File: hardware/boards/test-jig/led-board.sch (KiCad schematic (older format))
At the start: 22 parts

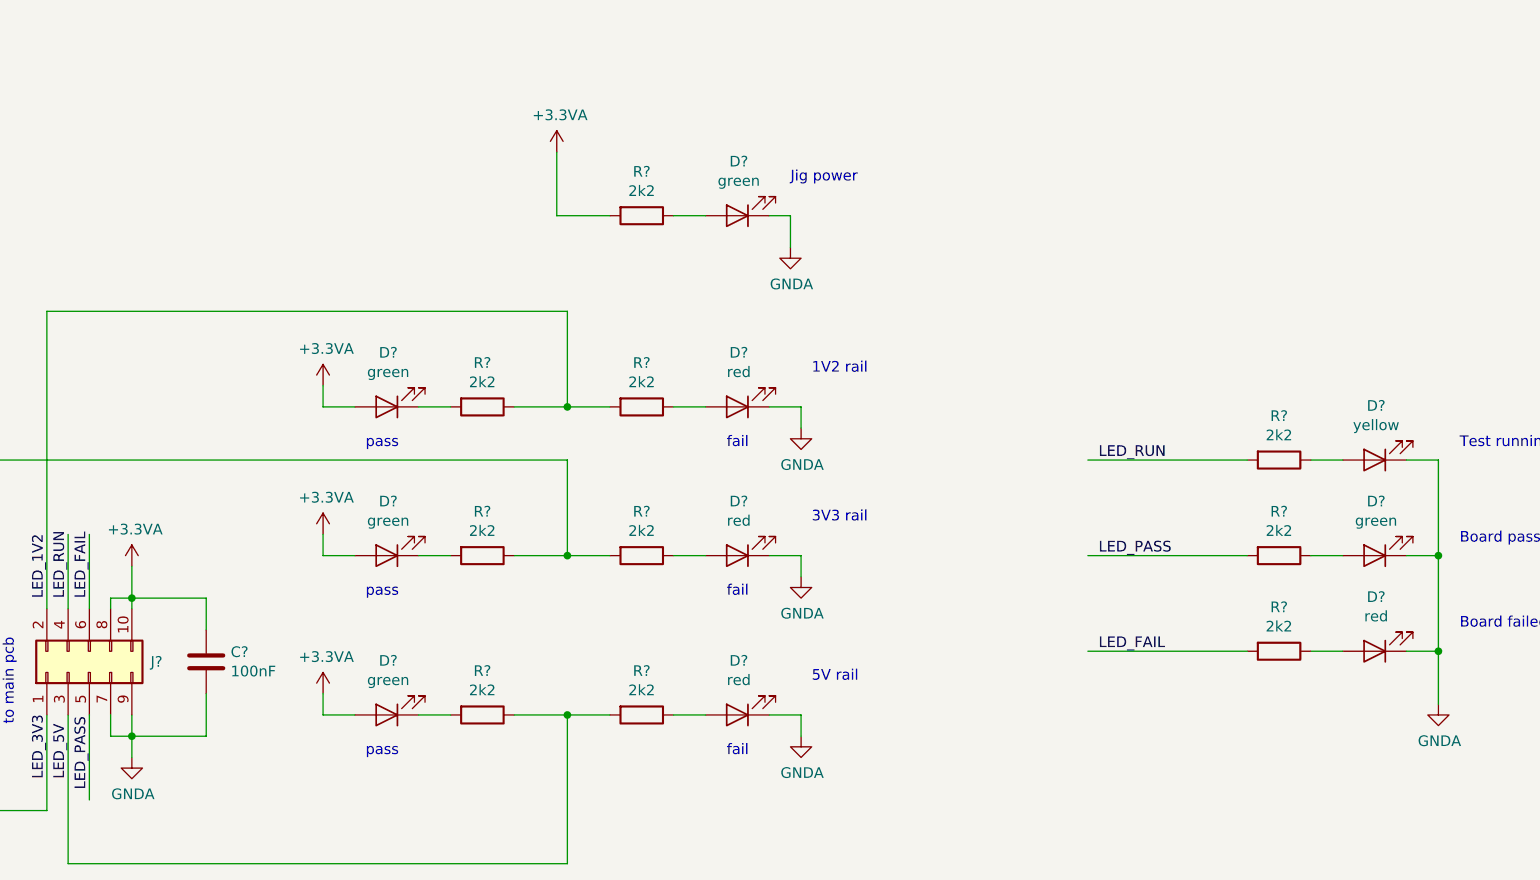
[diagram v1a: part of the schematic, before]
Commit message: test-jig schematics: annotate and ERC fixup
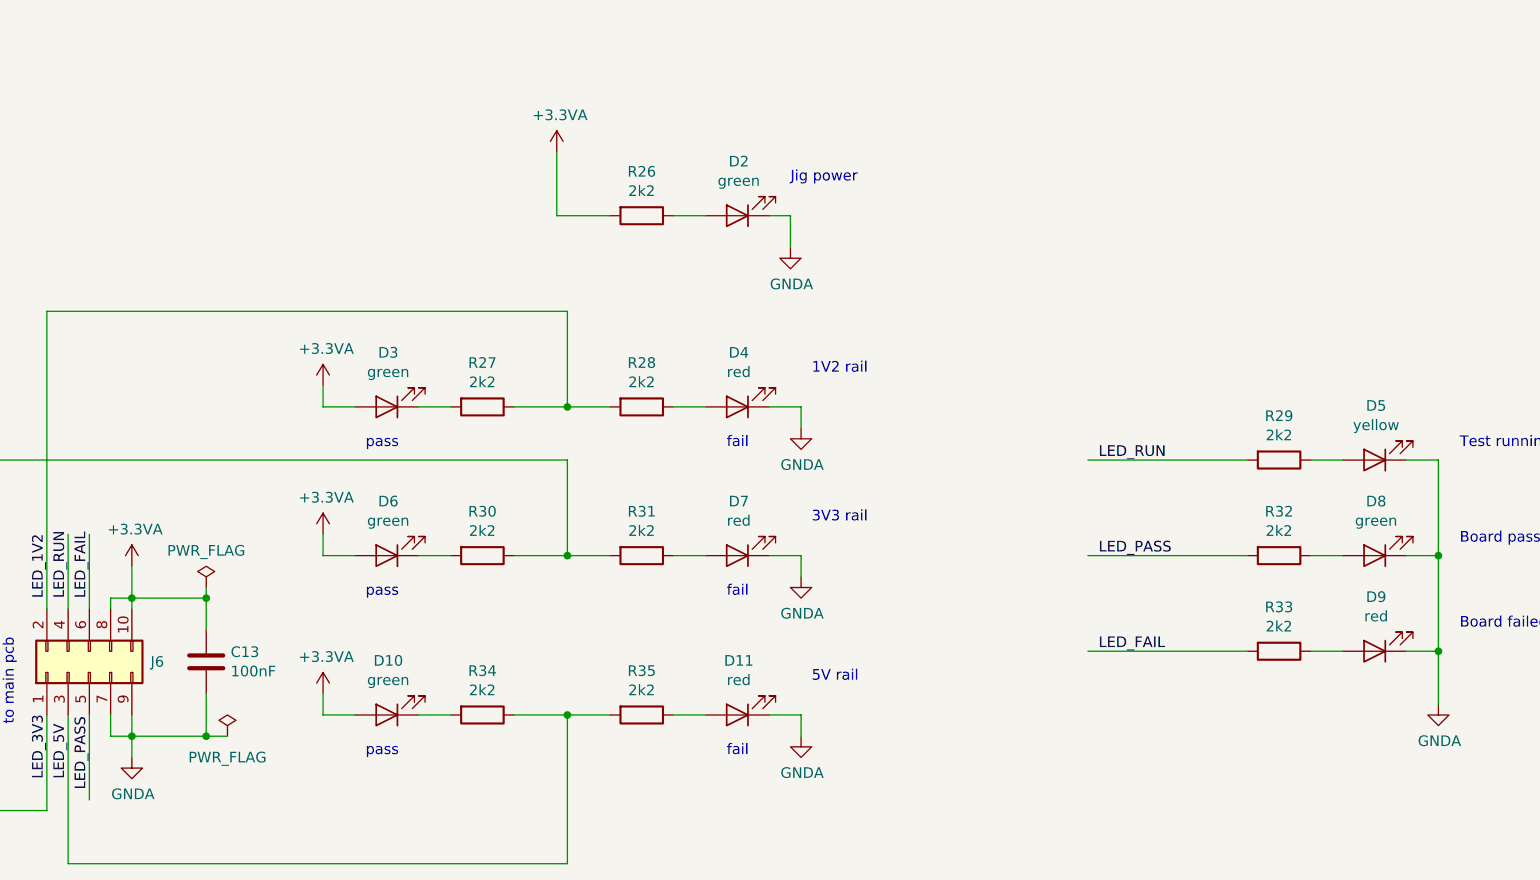
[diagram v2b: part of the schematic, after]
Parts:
- gave numbers to parts that had none: 22
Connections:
- wire segments 67 -> 69
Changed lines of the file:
@@
 Separate pcb for the LEDs for better visibility\nUse GNDA and 3.3VA to not connect any nets with the main pcb
 $Comp
-L Device:LED D?
+L Device:LED D2
 U 1 1 5D2DA011
 P 5300 2650
-F 0 "D?" H 5293 2395 50  0000 C CNN
+F 0 "D2" H 5293 2395 50  0000 C CNN
 F 1 "green" H 5293 2486 50  0000 C CNN
 F 2 "" H 5300 2650 50  0001 C CNN
@@
 $EndComp
 $Comp
-L power:+3.3VA #PWR?
+L power:+3.3VA #PWR043
 U 1 1 5D2DB5E9
 P 4450 2350
-F 0 "#PWR?" H 4450 2200 50  0001 C CNN
+F 0 "#PWR043" H 4450 2200 50  0001 C CNN
 F 1 "+3.3VA" H 4465 2523 50  0000 C CNN
 F 2 "" H 4450 2350 50  0001 C CNN
@@
 $EndComp
 $Comp
-L Device:R R?
+L Device:R R26
 U 1 1 5D2DBA07
 P 4850 2650
-F 0 "R?" V 4643 2650 50  0000 C CNN
+F 0 "R26" V 4643 2650 50  0000 C CNN
 F 1 "2k2" V 4734 2650 50  0000 C CNN
 F 2 "" V 4780 2650 50  0001 C CNN
@@
 $EndComp
 $Comp
-L power:GNDA #PWR?
+L power:GNDA #PWR044
 U 1 1 5D2DBC88
 P 5550 2800
-F 0 "#PWR?" H 5550 2550 50  0001 C CNN
+F 0 "#PWR044" H 5550 2550 50  0001 C CNN
 F 1 "GNDA" H 5555 2627 50  0000 C CNN
 F 2 "" H 5550 2800 50  0001 C CNN
@@
 LED_1V2
 $Comp
-L power:+3.3VA #PWR?
+L power:+3.3VA #PWR048
 U 1 1 5D2D6A47
 P 2450 4300
-F 0 "#PWR?" H 2450 4150 50  0001 C CNN
+F 0 "#PWR048" H 2450 4150 50  0001 C CNN
 F 1 "+3.3VA" H 2465 4473 50  0000 C CNN
 F 2 "" H 2450 4300 50  0001 C CNN
@@
 $EndComp
 $Comp
-L power:GNDA #PWR?
+L power:GNDA #PWR053
 U 1 1 5D2D645E
 P 2450 5200
-F 0 "#PWR?" H 2450 4950 50  0001 C CNN
+F 0 "#PWR053" H 2450 4950 50  0001 C CNN
 F 1 "GNDA" H 2455 5027 50  0000 C CNN
 F 2 "" H 2450 5200 50  0001 C CNN
@@
 P 2250 4800
 AR Path="/5D2D5562" Ref="J?"  Part="1"
-AR Path="/5D29701F/5D2D5562" Ref="J?"  Part="1"
-F 0 "J?" V 2300 4512 50  0000 R CNN
+AR Path="/5D29701F/5D2D5562" Ref="J6"  Part="1"
+F 0 "J6" V 2300 4512 50  0000 R CNN
 F 1 "Conn_02x05_Odd_Even" V 2255 4512 50  0001 R CNN
 F 2 "" H 2250 4800 50  0001 C CNN
@@
 $EndComp
 $Comp
-L Device:LED D?
+L Device:LED D4
 U 1 1 5D2E2982
 P 5300 3550
-F 0 "D?" H 5293 3295 50  0000 C CNN
+F 0 "D4" H 5293 3295 50  0000 C CNN
 F 1 "red" H 5293 3386 50  0000 C CNN
 F 2 "" H 5300 3550 50  0001 C CNN
@@
 $EndComp
 $Comp
-L Device:LED D?
+L Device:LED D3
 U 1 1 5D2E3538
 P 3650 3550
-F 0 "D?" H 3643 3295 50  0000 C CNN
+F 0 "D3" H 3643 3295 50  0000 C CNN
 F 1 "green" H 3643 3386 50  0000 C CNN
 F 2 "" H 3650 3550 50  0001 C CNN
@@
 $EndComp
 $Comp
-L Device:R R?
+L Device:R R27
 U 1 1 5D2E3CFF
 P 4100 3550
-F 0 "R?" V 3893 3550 50  0000 C CNN
+F 0 "R27" V 3893 3550 50  0000 C CNN
 F 1 "2k2" V 3984 3550 50  0000 C CNN
 F 2 "" V 4030 3550 50  0001 C CNN
@@
 $EndComp
 $Comp
-L Device:R R?
+L Device:R R28
 U 1 1 5D2E4301
 P 4850 3550
-F 0 "R?" V 4643 3550 50  0000 C CNN
+F 0 "R28" V 4643 3550 50  0000 C CNN
 F 1 "2k2" V 4734 3550 50  0000 C CNN
 F 2 "" V 4780 3550 50  0001 C CNN
@@
 $EndComp
 $Comp
-L power:GNDA #PWR?
+L power:GNDA #PWR046
 U 1 1 5D2E4E1B
 P 5600 3650
-F 0 "#PWR?" H 5600 3400 50  0001 C CNN
+F 0 "#PWR046" H 5600 3400 50  0001 C CNN
 F 1 "GNDA" H 5605 3477 50  0000 C CNN
 F 2 "" H 5600 3650 50  0001 C CNN
@@
 $EndComp
 $Comp
-L power:+3.3VA #PWR?
+L power:+3.3VA #PWR045
 U 1 1 5D2E5174
 P 3350 3450
-F 0 "#PWR?" H 3350 3300 50  0001 C CNN
+F 0 "#PWR045" H 3350 3300 50  0001 C CNN
 F 1 "+3.3VA" H 3365 3623 50  0000 C CNN
 F 2 "" H 3350 3450 50  0001 C CNN
@@
 fail
 $Comp
-L Device:LED D?
+L Device:LED D7
 U 1 1 5D2ED0DC
 P 5300 4250
-F 0 "D?" H 5293 3995 50  0000 C CNN
+F 0 "D7" H 5293 3995 50  0000 C CNN
 F 1 "red" H 5293 4086 50  0000 C CNN
 F 2 "" H 5300 4250 50  0001 C CNN
@@
 $EndComp
 $Comp
-L Device:LED D?
+L Device:LED D6
 U 1 1 5D2ED0E6
 P 3650 4250
-F 0 "D?" H 3643 3995 50  0000 C CNN
+F 0 "D6" H 3643 3995 50  0000 C CNN
 F 1 "green" H 3643 4086 50  0000 C CNN
 F 2 "" H 3650 4250 50  0001 C CNN
@@
 $EndComp
 $Comp
-L Device:R R?
+L Device:R R30
 U 1 1 5D2ED0F0
 P 4100 4250
-F 0 "R?" V 3893 4250 50  0000 C CNN
+F 0 "R30" V 3893 4250 50  0000 C CNN
 F 1 "2k2" V 3984 4250 50  0000 C CNN
 F 2 "" V 4030 4250 50  0001 C CNN
@@
 $EndComp
 $Comp
-L Device:R R?
+L Device:R R31
 U 1 1 5D2ED0FA
 P 4850 4250
-F 0 "R?" V 4643 4250 50  0000 C CNN
+F 0 "R31" V 4643 4250 50  0000 C CNN
 F 1 "2k2" V 4734 4250 50  0000 C CNN
 F 2 "" V 4780 4250 50  0001 C CNN
@@
 $EndComp
 $Comp
-L power:GNDA #PWR?
+L power:GNDA #PWR049
 U 1 1 5D2ED104
 P 5600 4350
-F 0 "#PWR?" H 5600 4100 50  0001 C CNN
+F 0 "#PWR049" H 5600 4100 50  0001 C CNN
 F 1 "GNDA" H 5605 4177 50  0000 C CNN
 F 2 "" H 5600 4350 50  0001 C CNN
@@
 $EndComp
 $Comp
-L power:+3.3VA #PWR?
+L power:+3.3VA #PWR047
 U 1 1 5D2ED10E
 P 3350 4150
-F 0 "#PWR?" H 3350 4000 50  0001 C CNN
+F 0 "#PWR047" H 3350 4000 50  0001 C CNN
 F 1 "+3.3VA" H 3365 4323 50  0000 C CNN
 F 2 "" H 3350 4150 50  0001 C CNN
@@
 	2050 3100 2050 4500
 $Comp
-L Device:LED D?
+L Device:LED D11
 U 1 1 5D2F33F7
 P 5300 5000
-F 0 "D?" H 5293 4745 50  0000 C CNN
+F 0 "D11" H 5293 4745 50  0000 C CNN
 F 1 "red" H 5293 4836 50  0000 C CNN
 F 2 "" H 5300 5000 50  0001 C CNN
@@
 $EndComp
 $Comp
-L Device:LED D?
+L Device:LED D10
 U 1 1 5D2F3401
 P 3650 5000
-F 0 "D?" H 3643 4745 50  0000 C CNN
+F 0 "D10" H 3643 4745 50  0000 C CNN
 F 1 "green" H 3643 4836 50  0000 C CNN
 F 2 "" H 3650 5000 50  0001 C CNN
@@
 $EndComp
 $Comp
-L Device:R R?
+L Device:R R34
 U 1 1 5D2F340B
 P 4100 5000
-F 0 "R?" V 3893 5000 50  0000 C CNN
+F 0 "R34" V 3893 5000 50  0000 C CNN
 F 1 "2k2" V 3984 5000 50  0000 C CNN
 F 2 "" V 4030 5000 50  0001 C CNN
@@
 $EndComp
 $Comp
-L Device:R R?
+L Device:R R35
 U 1 1 5D2F3415
 P 4850 5000
-F 0 "R?" V 4643 5000 50  0000 C CNN
+F 0 "R35" V 4643 5000 50  0000 C CNN
 F 1 "2k2" V 4734 5000 50  0000 C CNN
 F 2 "" V 4780 5000 50  0001 C CNN
@@
 $EndComp
 $Comp
-L power:GNDA #PWR?
+L power:GNDA #PWR052
 U 1 1 5D2F341F
 P 5600 5100
-F 0 "#PWR?" H 5600 4850 50  0001 C CNN
+F 0 "#PWR052" H 5600 4850 50  0001 C CNN
 F 1 "GNDA" H 5605 4927 50  0000 C CNN
 F 2 "" H 5600 5100 50  0001 C CNN
@@
 $EndComp
 $Comp
-L power:+3.3VA #PWR?
+L power:+3.3VA #PWR050
 U 1 1 5D2F3429
 P 3350 4900
-F 0 "#PWR?" H 3350 4750 50  0001 C CNN
+F 0 "#PWR050" H 3350 4750 50  0001 C CNN
 F 1 "+3.3VA" H 3365 5073 50  0000 C CNN
 F 2 "" H 3350 4900 50  0001 C CNN
@@
 	2150 5000 2150 5700
 $Comp
-L Device:C C?
+L Device:C C13
 U 1 1 5D2FCA51
 P 2800 4750
-F 0 "C?" H 2915 4796 50  0000 L CNN
+F 0 "C13" H 2915 4796 50  0000 L CNN
 F 1 "100nF" H 2915 4705 50  0000 L CNN
 F 2 "" H 2838 4600 50  0001 C CNN
@@
 	2800 5100 2800 4900
 $Comp
-L Device:LED D?
+L Device:LED D5
 U 1 1 5D3007CC
 P 8300 3800
-F 0 "D?" H 8293 3545 50  0000 C CNN
+F 0 "D5" H 8293 3545 50  0000 C CNN
 F 1 "yellow" H 8293 3636 50  0000 C CNN
 F 2 "" H 8300 3800 50  0001 C CNN
@@
 $EndComp
 $Comp
-L Device:LED D?
+L Device:LED D8
 U 1 1 5D300F42
 P 8300 4250
-F 0 "D?" H 8293 3995 50  0000 C CNN
+F 0 "D8" H 8293 3995 50  0000 C CNN
 F 1 "green" H 8293 4086 50  0000 C CNN
 F 2 "" H 8300 4250 50  0001 C CNN
@@
 $EndComp
 $Comp
-L Device:LED D?
+L Device:LED D9
 U 1 1 5D3015D6
 P 8300 4700
-F 0 "D?" H 8293 4445 50  0000 C CNN
+F 0 "D9" H 8293 4445 50  0000 C CNN
 F 1 "red" H 8293 4536 50  0000 C CNN
 F 2 "" H 8300 4700 50  0001 C CNN
@@
 $EndComp
 $Comp
-L power:GNDA #PWR?
+L power:GNDA #PWR051
 U 1 1 5D301917
 P 8600 4950
-F 0 "#PWR?" H 8600 4700 50  0001 C CNN
+F 0 "#PWR051" H 8600 4700 50  0001 C CNN
 F 1 "GNDA" H 8605 4777 50  0000 C CNN
 F 2 "" H 8600 4950 50  0001 C CNN
@@
 	8600 4700 8600 4950
 $Comp
-L Device:R R?
+L Device:R R29
 U 1 1 5D304A8F
 P 7850 3800
-F 0 "R?" V 7643 3800 50  0000 C CNN
+F 0 "R29" V 7643 3800 50  0000 C CNN
 F 1 "2k2" V 7734 3800 50  0000 C CNN
 F 2 "" V 7780 3800 50  0001 C CNN
@@
 $EndComp
 $Comp
-L Device:R R?
+L Device:R R32
 U 1 1 5D304C7B
 P 7850 4250
-F 0 "R?" V 7643 4250 50  0000 C CNN
+F 0 "R32" V 7643 4250 50  0000 C CNN
 F 1 "2k2" V 7734 4250 50  0000 C CNN
 F 2 "" V 7780 4250 50  0001 C CNN
@@
 $EndComp
 $Comp
-L Device:R R?
+L Device:R R33
 U 1 1 5D304F45
 P 7850 4700
-F 0 "R?" V 7643 4700 50  0000 C CNN
+F 0 "R33" V 7643 4700 50  0000 C CNN
 F 1 "2k2" V 7734 4700 50  0000 C CNN
 F 2 "" V 7780 4700 50  0001 C CNN
@@
 Text Notes 8700 4600 0    50   ~ 0
 Board failed
+$Comp
+L power:PWR_FLAG #FLG0102
+U 1 1 5D24D5EC
+P 2800 4400
+F 0 "#FLG0102" H 2800 4475 50  0001 C CNN
+F 1 "PWR_FLAG" H 2800 4573 50  0000 C CNN
+F 2 "" H 2800 4400 50  0001 C CNN
+F 3 "~" H 2800 4400 50  0001 C CNN
+	1    2800 4400
+	1    0    0    -1
+$EndComp
+Wire Wire Line
+	2800 4400 2800 4450
+Connection ~ 2800 4450
+$Comp
+L power:PWR_FLAG #FLG0103
+U 1 1 5D24FF06
+P 2900 5100
+F 0 "#FLG0103" H 2900 5175 50  0001 C CNN
+F 1 "PWR_FLAG" H 2900 5000 50  0000 C CNN
+F 2 "" H 2900 5100 50  0001 C CNN
+F 3 "~" H 2900 5100 50  0001 C CNN
+	1    2900 5100
+	1    0    0    -1
+$EndComp
+Wire Wire Line
+	2900 5100 2800 5100
+Connection ~ 2800 5100
 $EndSCHEMATC

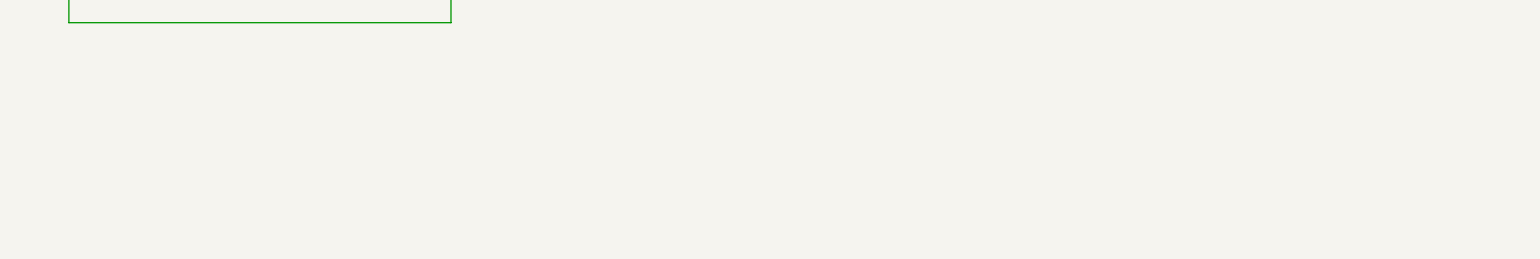
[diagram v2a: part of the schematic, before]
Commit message: test-jig schematics: small improvements
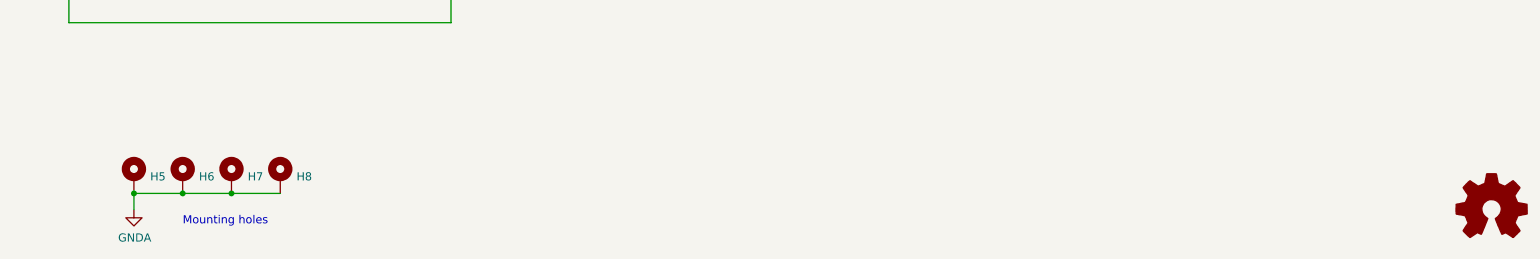
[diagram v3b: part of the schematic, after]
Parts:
- added H5, H6, H7, H8: MountingHole_Pad, symbol Mechanical:MountingHole_Pad
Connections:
- wire segments 69 -> 73
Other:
- note added: "Mounting holes"
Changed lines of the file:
@@
 Comment1 "License 0BSD or Apache 2.0"
 Comment2 ""
-Comment3 ""
+Comment3 "by Electronic Eel"
 Comment4 "Test Jig for Glasgow revC1"
 $EndDescr
@@
 	2900 5100 2800 5100
 Connection ~ 2800 5100
+$Comp
+L Mechanical:MountingHole_Pad H?
+U 1 1 5D2D86D9
+P 2550 6650
+AR Path="/5D2D86D9" Ref="H?"  Part="1"
+AR Path="/5D29701F/5D2D86D9" Ref="H5"  Part="1"
+F 0 "H5" H 2650 6653 50  0000 L CNN
+F 1 "MountingHole_Pad" H 2650 6608 50  0001 L CNN
+F 2 "" H 2550 6650 50  0001 C CNN
+F 3 "~" H 2550 6650 50  0001 C CNN
+	1    2550 6650
+	1    0    0    -1
+$EndComp
+$Comp
+L Mechanical:MountingHole_Pad H?
+U 1 1 5D2D86DF
+P 2850 6650
+AR Path="/5D2D86DF" Ref="H?"  Part="1"
+AR Path="/5D29701F/5D2D86DF" Ref="H6"  Part="1"
+F 0 "H6" H 2950 6653 50  0000 L CNN
+F 1 "MountingHole_Pad" H 2950 6608 50  0001 L CNN
+F 2 "" H 2850 6650 50  0001 C CNN
+F 3 "~" H 2850 6650 50  0001 C CNN
+	1    2850 6650
+	1    0    0    -1
+$EndComp
+$Comp
+L Mechanical:MountingHole_Pad H?
+U 1 1 5D2D86E5
+P 3150 6650
+AR Path="/5D2D86E5" Ref="H?"  Part="1"
+AR Path="/5D29701F/5D2D86E5" Ref="H7"  Part="1"
+F 0 "H7" H 3250 6653 50  0000 L CNN
+F 1 "MountingHole_Pad" H 3250 6608 50  0001 L CNN
+F 2 "" H 3150 6650 50  0001 C CNN
+F 3 "~" H 3150 6650 50  0001 C CNN
+	1    3150 6650
+	1    0    0    -1
+$EndComp
+$Comp
+L Mechanical:MountingHole_Pad H?
+U 1 1 5D2D86EB
+P 3450 6650
+AR Path="/5D2D86EB" Ref="H?"  Part="1"
+AR Path="/5D29701F/5D2D86EB" Ref="H8"  Part="1"
+F 0 "H8" H 3550 6653 50  0000 L CNN
+F 1 "MountingHole_Pad" H 3550 6608 50  0001 L CNN
+F 2 "" H 3450 6650 50  0001 C CNN
+F 3 "~" H 3450 6650 50  0001 C CNN
+	1    3450 6650
+	1    0    0    -1
+$EndComp
+Wire Wire Line
+	2550 6750 2850 6750
+Connection ~ 2550 6750
+Wire Wire Line
+	2850 6750 3150 6750
+Connection ~ 2850 6750
+Wire Wire Line
+	3150 6750 3450 6750
+Connection ~ 3150 6750
+Text Notes 2850 6950 0    50   ~ 0
+Mounting holes
+$Comp
+L power:GNDA #PWR074
+U 1 1 5D2DA549
+P 2550 6850
+F 0 "#PWR074" H 2550 6600 50  0001 C CNN
+F 1 "GNDA" H 2555 6677 50  0000 C CNN
+F 2 "" H 2550 6850 50  0001 C CNN
+F 3 "" H 2550 6850 50  0001 C CNN
+	1    2550 6850
+	1    0    0    -1
+$EndComp
+Wire Wire Line
+	2550 6750 2550 6850
+$Comp
+L Graphic:Logo_Open_Hardware_Small #LOGO2
+U 1 1 5D2E9FD2
+P 10900 6850
+F 0 "#LOGO2" H 10900 7125 50  0001 C CNN
+F 1 "Logo_Open_Hardware_Small" H 10900 6625 50  0001 C CNN
+F 2 "" H 10900 6850 50  0001 C CNN
+F 3 "~" H 10900 6850 50  0001 C CNN
+	1    10900 6850
+	1    0    0    -1
+$EndComp
 $EndSCHEMATC
